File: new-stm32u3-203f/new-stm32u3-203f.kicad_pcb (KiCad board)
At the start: 4 copper layers, 14.5 x 80 mm, 88 parts, among them J1 Display, J2 SJ-3524-SMT, J3 12401826E412A, J4 Battery connector, J5 473092651, J6 UART, SW1 SW_SPDT, SW2 SW_SPDT, SW3 VOL+, SW4 VOL-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

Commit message: made some progress on the pcb layout
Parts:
- removed R18: 10k, Resistor_SMD:R_0603_1608Metric
- removed SW7: Menu, Button_Switch_SMD:Panasonic_EVQPUL_EVQPUC
- C20: moved to B.Cu
- moved C20 66.1 mm to (191.0, 143.0), turned to 180 degrees
- moved J4 50.4 mm to (163.8, 132.8)
- moved CR3 14.6 mm to (193.5, 141.8), turned to -90 degrees
- moved C19 10.8 mm to (190.8, 145.8)
- moved J3 10.8 mm to (191.2, 154.8)
- moved CR1 10.6 mm to (186.9, 147.0)
- moved CR2 10.5 mm to (190.5, 147.5)
- moved U6 10.0 mm to (191.7, 136.5)
- moved U3 10.0 mm to (195.3, 146.0)
- moved U7 9.98 mm to (195.8, 140.5)
- moved MOSFET1 9.53 mm to (187.0, 142.0), turned to -90 degrees
- moved U5 9.29 mm to (187.8, 136.6), turned to -90 degrees
- moved U4 8.42 mm to (195.8, 136.3)
- moved X1 0.79 mm to (186.8, 125.2)
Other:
- board size 14.5 x 80 mm -> 14.5 x 90 mm

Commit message: made some progress witht he layout.
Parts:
- removed R5: 0R, Resistor_SMD:R_0603_1608Metric
- 1V8: renamed from TP3; moved to B.Cu
- 3V3: renamed from TP1; moved to B.Cu
- 5V: renamed from TP2; moved to B.Cu
- C26, C27, C28, C29, C30, C31, J4, J6, L2, R3, R4, R6, R7: moved to B.Cu
- moved R3 70.3 mm to (197.5, 148.0), turned to -90 degrees
- moved C26 68.8 mm to (195.0, 140.5), turned to 180 degrees
- moved C27 66.9 mm to (195.0, 139.0), turned to 180 degrees
- moved C28 63.2 mm to (195.0, 131.8), turned to 180 degrees
- moved C29 62.9 mm to (195.0, 133.5), turned to 180 degrees
- moved C30 60.4 mm to (191.0, 139.7), turned to 180 degrees
- moved 5V 60.1 mm to (197.5, 139.2), turned to 180 degrees
- moved R4 59.5 mm to (191.0, 141.2)
- moved 3V3 59.3 mm to (197.5, 133.2), turned to 180 degrees
- moved C31 58.0 mm to (187.3, 139.0), turned to 180 degrees
- moved L2 53.7 mm to (187.3, 137.2), turned to 180 degrees
- moved R6 49.2 mm to (187.5, 135.5), turned to 180 degrees
- moved R7 47.1 mm to (185.0, 138.3), turned to -90 degrees
- moved 1V8 46.3 mm to (185.0, 135.5), turned to 180 degrees
- moved U6 19.8 mm to (172.0, 138.1)
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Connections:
- 5V pad 1: USB_3v3_EN -> 5V_UCPD
- C26 pad 2: USB_3v3_EN -> 5V_UCPD
- C27 pad 2: USB_3v3_EN -> 5V_UCPD
- U4 pad 1: USB_3v3_EN -> 5V_UCPD
- U4 pad 6: USB_3v3_EN -> 5V_UCPD

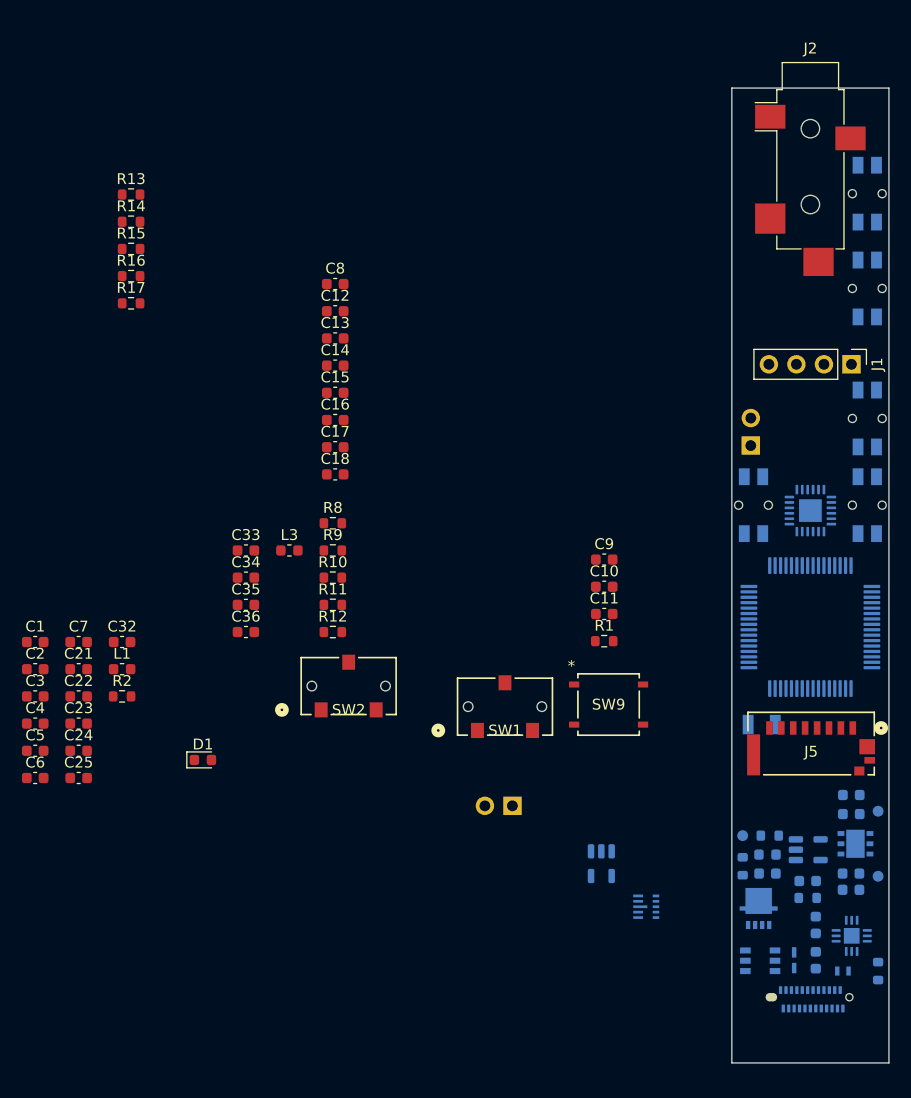
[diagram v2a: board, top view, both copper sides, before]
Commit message: moved over to just using direct usb 2.0, made progress on pcb layout
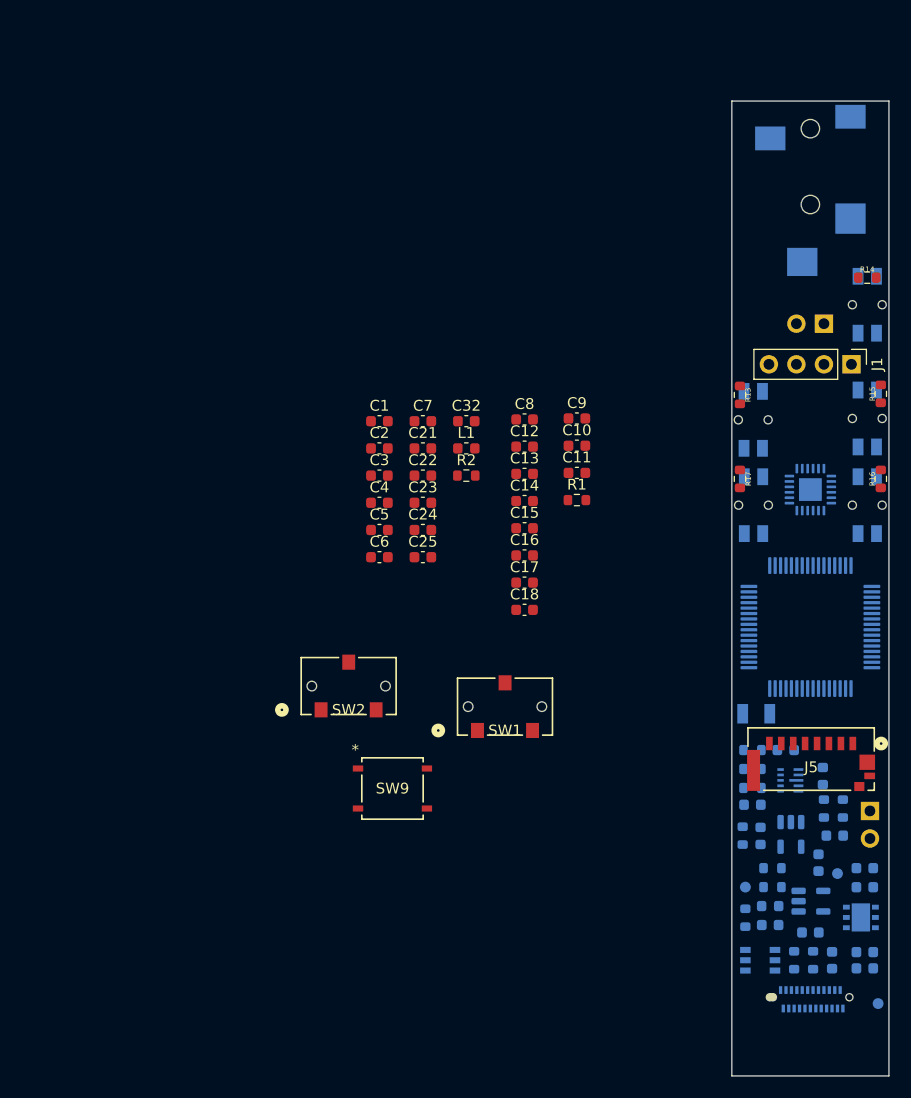
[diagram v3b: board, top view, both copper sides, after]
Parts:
- removed C20: 100n, Capacitor_SMD:C_0603_1608Metric
- removed CR2: ESDA25P35-1U1M, footprints_esda25:QFN1610_STM
- removed CR3: BAT54KFILM, footprints_BAT54:SOD-523_STM
- removed MOSFET1: STL11N3LLH6, footprints_stl11n3:POWERFLAT-3p3X3p3_STM
- removed U3: TCPP01-M12, Package_DFN_QFN:QFN-12-1EP_3x3mm_P0.5mm_EP1.45x1.45mm
- added R18: 5K1, Resistor_SMD:R_0603_1608Metric, B.Cu at (189.8, 147.0)
- added R5: 5K1, Resistor_SMD:R_0603_1608Metric, B.Cu at (191.5, 147.0)
- C33, C34, C35, C36, D1, J2, L3, R10, R11, R12, R8, R9: moved to B.Cu
- R3: value 2K4 -> 202k
- R4: value 10K -> 202k
- moved R16 71.7 mm to (197.8, 102.6), turned to 90 degrees
- moved R15 70.5 mm to (197.8, 94.7), turned to 90 degrees
- moved R14 68.1 mm to (196.5, 84.0)
- moved C33 60.2 mm to (192.0, 138.0), turned to -90 degrees
- moved C34 59.3 mm to (193.5, 135.5), turned to 180 degrees
- moved R13 59.2 mm to (184.8, 94.8), turned to -90 degrees
- moved R17 58.5 mm to (184.8, 102.6), turned to -90 degrees
- moved L3 53.5 mm to (192.4, 130.0), turned to -90 degrees
- moved D1 51.9 mm to (186.7, 135.5), turned to -90 degrees
- moved R8 51.6 mm to (187.8, 138.5), turned to 180 degrees
- moved C36 51.0 mm to (189.0, 127.6), turned to 180 degrees
- moved C35 50.3 mm to (185.9, 132.7)
- moved R9 46.1 mm to (185.0, 135.5), turned to -90 degrees
- moved R10 43.3 mm to (185.9, 131.1), turned to 180 degrees
- moved R11 41.6 mm to (185.9, 129.3), turned to 180 degrees
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- renumbered 3V3 to TP1, 5V to TP2, 1V8 to TP3
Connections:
- C19 pad 1: USB_VBUS -> USB_3v3_EN
- C26 pad 2: 5V_UCPD -> USB_3v3_EN
- C27 pad 2: 5V_UCPD -> USB_3v3_EN
- C33 pad 2: USB_VBUS -> USB_3v3_EN
- J3 pad A4: USB_VBUS -> USB_3v3_EN
- J3 pad A9: USB_VBUS -> USB_3v3_EN
- J3 pad B4: USB_VBUS -> USB_3v3_EN
- J3 pad B9: USB_VBUS -> USB_3v3_EN
- R3 pad 1: GNDREF -> +BATT
- R3 pad 2: Net-(U3-VBUS_CTRL) -> BATT_MON
- R4 pad 1: USB_VBUS -> GNDREF
- R4 pad 2: Net-(U3-VBUS_CTRL) -> BATT_MON
- R8 pad 2: USB_VBUS -> USB_3v3_EN
- TP2 pad 1: 5V_UCPD -> USB_3v3_EN
- U1 pad 25: unconnected-(U1A-PB1-Pad25) -> BATT_MON
- U4 pad 1: 5V_UCPD -> USB_3v3_EN
- U4 pad 6: 5V_UCPD -> USB_3v3_EN
- U6 pad 4: USB_VBUS -> USB_3v3_EN

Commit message: finished the layout of the pcb
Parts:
- removed C32: 4.7u, Capacitor_SMD:C_0603_1608Metric
- removed R2: 0R, Resistor_SMD:R_0603_1608Metric
- removed SW2: SW_SPDT, footprints_SPDT_slide:CL-SB-12B-01_NDC
- C12, C13, C14, C15, C16, C17, C18, C22, C23, C24, C3, C4, C5, C6, C7, L1, SW9: moved to B.Cu
- SW1: footprint footprints_SPDT_slide:CL-SB-12B-01_NDC -> switch:SW_CJS-1200TA
- X1: moved to F.Cu
- moved SW1 49.5 mm to (149.5, 76.0), turned to -90 degrees
- moved L3 39.0 mm to (154.0, 123.2)
- moved U7 38.2 mm to (151.9, 123.2)
- moved C19 37.7 mm to (156.2, 139.7)
- moved C26 37.7 mm to (159.3, 140.4)
- moved C27 37.7 mm to (159.3, 138.9)
- moved C28 37.7 mm to (159.3, 131.2)
- moved C30 37.7 mm to (154.2, 137.1)
- moved C31 37.7 mm to (150.5, 136.4)
- moved C33 37.7 mm to (155.0, 130.7)
- moved C34 37.7 mm to (156.5, 128.2)
- moved C35 37.7 mm to (148.9, 125.3)
- moved CR1 37.7 mm to (149.6, 139.7)
- moved D1 37.7 mm to (149.7, 128.2)
- moved J3 37.7 mm to (154.2, 147.4)
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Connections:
- C10 pad 2: GNDREF -> GNDA
- C11 pad 2: GNDREF -> GNDA
- C14 pad 2: GNDREF -> GNDA
- C15 pad 1: GNDREF -> GNDA
- C16 pad 1: GNDREF -> GNDA
- C17 pad 1: GNDREF -> GNDA
- C18 pad 1: GNDREF -> GNDA
- C19 pad 2: GNDREF -> GNDA
- C21 pad 1: GNDREF -> GNDA
- C22 pad 1: GNDREF -> GNDA
- C23 pad 1: GNDREF -> GNDA
- C24 pad 1: GNDREF -> GNDA
- C25 pad 1: GNDREF -> GNDA
- C26 pad 1: GNDREF -> GNDA
- C27 pad 1: GNDREF -> GNDA
- C28 pad 1: GNDREF -> GNDA
- C29 pad 1: GNDREF -> GNDA
- C3 pad 2: GNDREF -> GNDA
- C30 pad 1: GNDREF -> GNDA
- C31 pad 1: GNDREF -> GNDA
- C33 pad 1: GNDREF -> GNDA
- C34 pad 1: GNDREF -> GNDA
- C35 pad 1: GNDREF -> GNDA
- C36 pad 1: GNDREF -> GNDA
- C4 pad 2: GNDREF -> GNDA
- C5 pad 1: GNDREF -> GNDA
- C6 pad 1: GNDREF -> GNDA
- C7 pad 1: GNDREF -> GNDA
- C8 pad 1: GNDREF -> GNDA
- C9 pad 1: GNDREF -> GNDA
- CR1 pad 2: GNDREF -> GNDA
- J1 pad 4: GNDREF -> GNDA
- J4 pad 1: GNDREF -> GNDA
- J4 pad 2: Net-(J4-Pin_2) -> +BATT
- J5 pad 6: GNDREF -> GNDA
- J5 pad G1: GNDREF -> GNDA
- J5 pad G2: GNDREF -> GNDA
- J5 pad G3: GNDREF -> GNDA
- J5 pad G4: GNDREF -> GNDA
- R10 pad 2: GNDREF -> GNDA
- R13 pad 2: GNDREF -> GNDA
- R14 pad 2: GNDREF -> GNDA
- R15 pad 2: GNDREF -> GNDA
- R16 pad 2: GNDREF -> GNDA
- R17 pad 2: GNDREF -> GNDA
- R18 pad 2: GNDREF -> GNDA
- R4 pad 1: GNDREF -> GNDA
- R5 pad 2: GNDREF -> GNDA
- R7 pad 2: GNDREF -> GNDA
- R9 pad 1: GNDREF -> GNDA
- SW1 pad 1: GNDREF -> GNDA
- SW9 pad 1: GNDREF -> GNDA
- U1 pad 18: GNDREF -> GNDA
- U1 pad 30: GNDREF -> GNDA
- U1 pad 32: GNDREF -> GNDA
- U1 pad 47: GNDREF -> GNDA
- U1 pad 63: GNDREF -> GNDA
- U2 pad 14: GNDREF -> GNDA
- U2 pad 21: GNDREF -> GNDA
- U2 pad 23: GNDREF -> GNDA
- U4 pad 2: GNDREF -> GNDA
- U4 pad 7: GNDREF -> GNDA
- U5 pad 2: GNDREF -> GNDA
- U6 pad 2: GNDREF -> GNDA
- U7 pad 2: GNDREF -> GNDA
- U7 pad 3: GNDREF -> GNDA
- U7 pad 8: GNDREF -> GNDA

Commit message: made some progress on layout and routes.
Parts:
- C12, C13: moved to F.Cu
- C21, C25: moved to B.Cu
- moved C12 19.9 mm to (149.8, 69.8)
- moved C13 18.0 mm to (160.5, 72.8)
- moved SW9 8.09 mm to (166.0, 118.8)
- moved L1 4.77 mm to (153.2, 117.2), turned to 90 degrees
- moved C21 3.92 mm to (155.8, 101.0), turned to 0 degrees
- moved C6 3.62 mm to (150.5, 118.2), turned to 0 degrees
- moved C36 3.56 mm to (148.9, 122.1)
- moved R11 3.47 mm to (152.0, 120.5), turned to 0 degrees
- moved C22 3.29 mm to (157.2, 116.8)
- moved C16 2.42 mm to (153.5, 99.0), turned to 90 degrees
- moved C4 2.32 mm to (148.2, 117.8), turned to 90 degrees
- moved C11 2.04 mm to (157.0, 105.9), turned to 180 degrees
- moved R9 2.02 mm to (150.0, 128.5)
- moved U2 2.01 mm to (154.2, 94.2)
- moved C23 1.95 mm to (155.8, 99.5), turned to 0 degrees
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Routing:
- net AVDD: track 0.00 -> 28.7 mm
- net GNDA: track 0.00 -> 22.7 mm
- net LDOIN: track 0.00 -> 16.1 mm
- net +BATT: track 0.00 -> 10.7 mm
- net V11: track 0.00 -> 10.4 mm
- net USB_3v3_EN: track 0.00 -> 6.53 mm
- net Net-(U7-FB): track 0.00 -> 5.53 mm
- net Net-(U2-AVDD): track 0.00 -> 3.90 mm
- net Net-(D1-K): track 0.00 -> 3.70 mm
- net Net-(U2-REF): track 0.00 -> 3.61 mm
- net STAT: track 0.00 -> 2.98 mm
- net Net-(U7-PG): track 0.00 -> 2.53 mm
- net /MCU_IO/SW_BOOT: track 0.00 -> 2.38 mm
- net OSC_OUT: track 0.00 -> 2.30 mm
- net VLX: track 0.00 -> 2.15 mm
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- added copper zone on In1.Cu, net GNDA

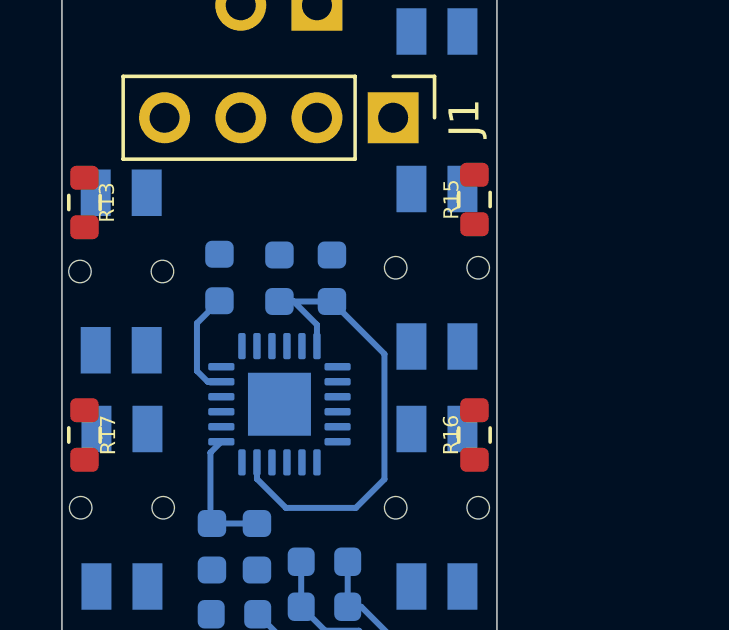
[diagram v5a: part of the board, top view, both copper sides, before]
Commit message: added in 0r to choose ldoin of dac
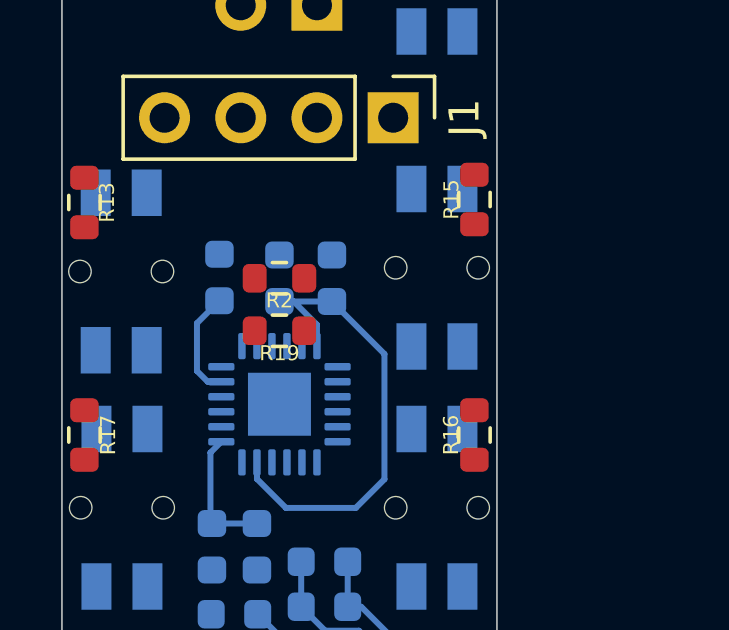
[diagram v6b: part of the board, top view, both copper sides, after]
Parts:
- added R19: 0R, Resistor_SMD:R_0603_1608Metric, F.Cu at (154.2, 91.8)
- added R2: 0R, Resistor_SMD:R_0603_1608Metric, F.Cu at (154.2, 90.0)
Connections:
- C17 pad 2: LDOIN -> +1V8
- C18 pad 2: LDOIN -> +1V8
- C31 pad 2: LDOIN -> +1V8
- L2 pad 2: LDOIN -> +1V8
- R6 pad 1: LDOIN -> +1V8
- TP3 pad 1: LDOIN -> +1V8
- U2 pad 11: LDOIN -> Net-(U2-LDOIN/HPVDD)
- U2 pad 22: LDOIN -> +1V8
- U2 pad 24: LDOIN -> +1V8
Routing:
- net LDOIN: track 16.1 -> 0.00 mm
- net (no net): track 0.00 -> 16.1 mm

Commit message: made routing progress
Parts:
- C12, C13: moved to B.Cu
- C15, C17: value 0.1u -> 1u
- moved C12 2.30 mm to (148.0, 68.2), turned to -90 degrees
- moved C13 0.75 mm to (160.5, 73.5), turned to -90 degrees
- moved C17 0.30 mm to (154.2, 89.8)
- moved C18 0.30 mm to (156.0, 89.8)
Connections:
- J2 pad R: (no net) -> Net-(J2-R)
- J2 pad S: (no net) -> GNDA
- J2 pad T: (no net) -> Net-(J2-L)
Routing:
- net (no net): track 16.1 -> 0.00 mm
- net GNDA: track 22.7 -> 30.4 mm
- net +1V8: track 0.00 -> 3.89 mm
- net Net-(J2-R): track 0.00 -> 3.68 mm
- net Net-(J2-L): track 0.00 -> 2.75 mm

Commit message: made some better progress routing
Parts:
- removed SW9: SW_RST, footprints_RST_BTN:SON4_PTS526 SM15 SMTR2 LFS_CNK
- added J7: RESET, Connector_PinHeader_1.00mm:PinHeader_1x02_P1.00mm_Vertical, F.Cu at (156.5, 140.3)
- moved C19 7.46 mm to (160.2, 146.0)
- moved R5 2.08 mm to (152.8, 138.6), turned to 90 degrees
- moved R18 1.75 mm to (154.5, 139.8), turned to 90 degrees
- moved C30 0.98 mm to (155.2, 137.0)
- moved TP2 0.95 mm to (160.2, 142.8)
- moved C31 0.55 mm to (150.5, 137.0)
- moved C5 0.40 mm to (150.5, 116.9)
- moved L1 0.35 mm to (152.9, 117.3)
- moved C6 0.25 mm to (150.5, 118.5)
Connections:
- J2 pad R: Net-(J2-R) -> (no net)
- J2 pad S: GNDA -> (no net)
- J2 pad T: Net-(J2-L) -> (no net)
- R2 pad 2: unconnected-(R2-Pad2) -> Net-(U2-LDOIN/HPVDD)
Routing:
- net AVDD: track 28.7 -> 197.0 mm, vias 0 -> 4
- net +1V8: track 3.89 -> 72.2 mm, vias 0 -> 1
- net sk_btn_2: track 0.00 -> 61.2 mm, vias 0 -> 6
- net UART_TX: track 0.00 -> 53.2 mm, vias 0 -> 1
- net USB_D-: track 0.00 -> 52.5 mm, vias 0 -> 4
- net SD_DAT2: track 0.00 -> 47.6 mm, vias 0 -> 4
- net UBS_D+: track 0.00 -> 47.4 mm, vias 0 -> 2
- net UART_RX: track 0.00 -> 45.5 mm, vias 0 -> 1
- net ps_btn_1: track 0.00 -> 43.1 mm, vias 0 -> 5
- net SD_DAT3: track 0.00 -> 42.5 mm, vias 0 -> 3
- net USB_3v3_EN: track 6.53 -> 47.7 mm, vias 0 -> 2
- net /MCU_IO/NRST: track 0.00 -> 37.5 mm, vias 0 -> 3
- net HP_RIGHT: track 0.00 -> 33.9 mm, vias 0 -> 2
- net v+_btn_3: track 0.00 -> 33.1 mm, vias 0 -> 5
- net DAC_RST: track 0.00 -> 32.0 mm, vias 0 -> 2
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- removed copper zone on In1.Cu, net GNDA
